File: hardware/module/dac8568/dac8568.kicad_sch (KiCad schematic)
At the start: 5 parts

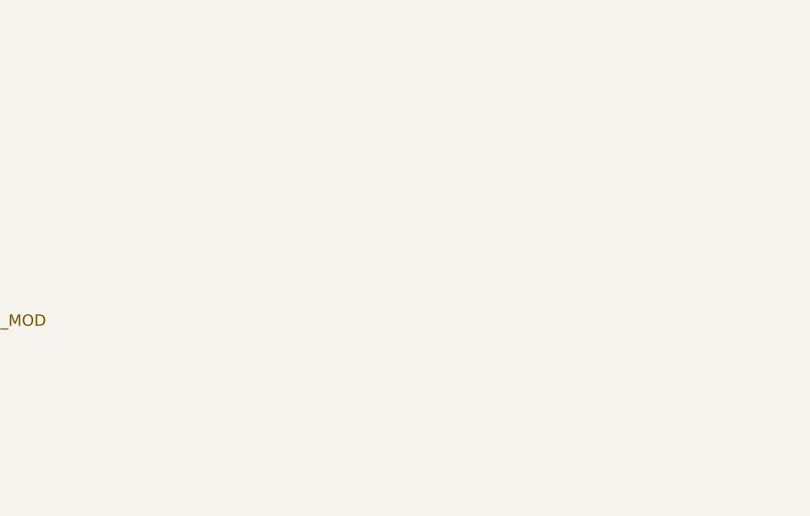
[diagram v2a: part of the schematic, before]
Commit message: Module: VREFOUT gets its 100 nF, breath-receive open items settled; module sims re-run on the changed netlists
C-VREF-DAC is SBAS430E p.31's minimum 100 nF at the reference pin; the
dac8568 page records that the pin is 3-state until firmware enables the
reference and TRIM-OFFSET holds it at 0 V. R-ZERO-TOP documented on the
breath receive page. power-entry, umbilical-load-switch, pitch-stage and
breath-receive-stage sims re-run: all assertions pass.

Co-Authored-By: Claude Opus 5.5 <noreply@anthropic.com>
Claude-Session: https://claude.ai/code/session_01LmB4muFXnoLprWX4JzuJ5A
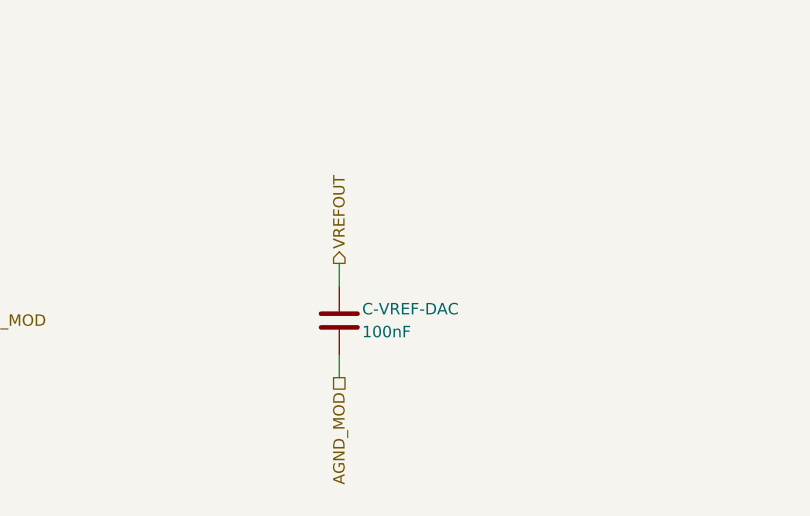
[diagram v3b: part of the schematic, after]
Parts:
- added C-VREF-DAC: 100nF, Capacitor_SMD:C_0805_2012Metric, symbol Device:C
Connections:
- net AGND_MOD: now also C-VREF-DAC.2
- net VREFOUT: now also C-VREF-DAC.1
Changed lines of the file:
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@@
     (property "Figure" "dig-gnd-topology" (at 142.24 148.59 0) (effects (font (size 1.27 1.27)) hide)))
   (text "FROM THE HAND-WRITTEN NETLIST THIS SHEET REPLACES (verbatim; the part notes are on each part's Note field):\n\nA LONE NO-CONNECT PIN'S NET IS NAMED AFTER THE PIN (the export names it so, whatever label it carries), so the\none-pin nets the text below names are, on this sheet: DAC_CH6_UNUSED is VOUTF; DAC_CH8_UNUSED is VOUTH.\n\nAUTHORITATIVE for connectivity. The ASCII drawing in dac8568.md is a REPRESENTATION of this file.\n\nTHE DRAWING SHOWS TWO PINS OF SIXTEEN. It was split out of digital-and-supervision.md to carry the CLR and\nLDAC corrections, and those are all it draws - the SPI pins, the rail, the ground and all six live outputs are\nprose in the ## Interfaces table and nowhere in the picture. They are netted here. That gap is the reason a\nnetlist is worth more than a redraw: a picture of two pins cannot be wrong about the other fourteen, and it\ncannot be right about them either.\n\nPin names are SBAS430E's own, from the 16-pin TSSOP PIN DESCRIPTIONS table of the banked\ndatasheets/analog/DAC8568CIPW.pdf [datasheet]: 1 LDAC   2 SYNC   3 AVDD   4 VOUTA  5 VOUTC  6 VOUTE  7 VOUTG 8\nVREFIN/VREFOUT  9 CLR   10 VOUTH 11 VOUTF 12 VOUTD 13 VOUTB 14 GND  15 DIN   16 SCLK\n\n[pins] CHANNEL NUMBER TO DATASHEET LETTER IS ORDINAL HERE: ch1=VOUTA through ch8=VOUTH, so the two spares are\nVOUTF and VOUTH. NO DOCUMENT IN THIS CORPUS STATES THAT MAP [derived, not cited] - ADR 0006 allocates by\nnumber and the datasheet names by letter, and nothing joins them. It is the only reading consistent with\n\"channels 6 and 8 spare\", and it decides which two pins a layout leaves unconnected, so it is asserted here\nrather than left implied. Contradict it in ADR 0006 if it is wrong and this file follows.\n\n[LDAC] LOCAL, and it crosses no boundary: the pin and its strap, nothing else. That is the whole content of\nthe LDAC correction.\n\n[VOUTF] THE TWO SPARES, NAMED SO THEY ARE NO-CONNECT BY DECISION RATHER THAN BY OMISSION. An unlisted pin and\na pin listed as going nowhere read the same in a picture and not at all the same in a layout review.\n\nNets with one endpoint on purpose." (at 256.54 38.099999999999994 0) (effects (font (size 1.27 1.27)) (justify left top)))
+  (symbol (lib_id "Device:C") (at 243.84 142.24 0) (unit 1)
+    (in_bom yes) (on_board yes) (dnp no)
+    (property "Reference" "C-VREF-DAC" (at 246.38 140.97 0) (effects (font (size 1.27 1.27)) (justify left)))
+    (property "Value" "100nF" (at 246.38 143.51 0) (effects (font (size 1.27 1.27)) (justify left)))
+    (property "Footprint" "Capacitor_SMD:C_0805_2012Metric" (at 243.84 142.24 0) (effects (font (size 1.27 1.27)) hide))
+    (property "Datasheet" "" (at 243.84 142.24 0) (effects (font (size 1.27 1.27)) hide))
+    (property "Row" "C-VREF-DAC" (at 243.84 142.24 0) (effects (font (size 1.27 1.27)) hide))
+    (property "Pins" "1=1 2=2" (at 243.84 142.24 0) (effects (font (size 1.27 1.27)) hide))
+    (property "Note" "VREFIN/VREFOUT to AGND_MOD at the pin: 'A minimum 100nF capacitor is recommended between the reference output and GND for noise filtering' (SBAS430E p.31)" (at 243.84 142.24 0) (effects (font (size 1.27 1.27)) hide))
+    (property "Manufacturer" "YAGEO" (at 243.84 142.24 0) (effects (font (size 1.27 1.27)) hide))
+    (property "MPN" "CC0805KRX7R9BB104" (at 243.84 142.24 0) (effects (font (size 1.27 1.27)) hide))
+    (property "LCSC" "C49678" (at 243.84 142.24 0) (effects (font (size 1.27 1.27)) hide))
+    (property "Assembly" "machine" (at 243.84 142.24 0) (effects (font (size 1.27 1.27)) hide))
+    (pin "1")
+    (pin "2")
+    (instances (project "module-main" (path "/fc77e9f9-9171-5c83-92ae-8cafe880764e/d3416dad-1f82-5e64-9a2d-7d16a2560a26" (reference "C43") (unit 1))) (project "dac8568" (path "/b85ef4e1-b1b5-5711-b0e7-36990bb72a4d" (reference "C-VREF-DAC") (unit 1))))
+  )
+  (wire (pts (xy 243.84 138.43) (xy 243.84 135.89)) (stroke (width 0) (type default)))
+  (hierarchical_label "VREFOUT" (shape output) (at 243.84 135.89 90) (effects (font (size 1.27 1.27)) (justify left))
+    (property "Dir" "out" (at 243.84 135.89 0) (effects (font (size 1.27 1.27)) hide))
+    (property "To" "module/pitch-stage" (at 243.84 135.89 0) (effects (font (size 1.27 1.27)) hide)))
+  (wire (pts (xy 243.84 146.05) (xy 243.84 148.59)) (stroke (width 0) (type default)))
+  (hierarchical_label "AGND_MOD" (shape passive) (at 243.84 148.59 270) (effects (font (size 1.27 1.27)) (justify right))
+    (property "Dir" "ref" (at 243.84 148.59 0) (effects (font (size 1.27 1.27)) hide))
+    (property "From" "module/power-entry" (at 243.84 148.59 0) (effects (font (size 1.27 1.27)) hide))
+    (property "Figure" "dig-gnd-topology" (at 243.84 148.59 0) (effects (font (size 1.27 1.27)) hide)))
   (sheet_instances (path "/" (page "1")))
 )
